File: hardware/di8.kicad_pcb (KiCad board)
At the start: 4 copper layers, 100 x 85 mm, 128 parts, among them J101 TNG-Power-TOP, J102 TNG-Power-BTM, J103 TNG-Data-TOP, J104 TNG-Data-BTM, P101 BOOT, P102 Debug, P103 PE, P201 INPUT0, P202 INPUT1, P203 INPUT2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

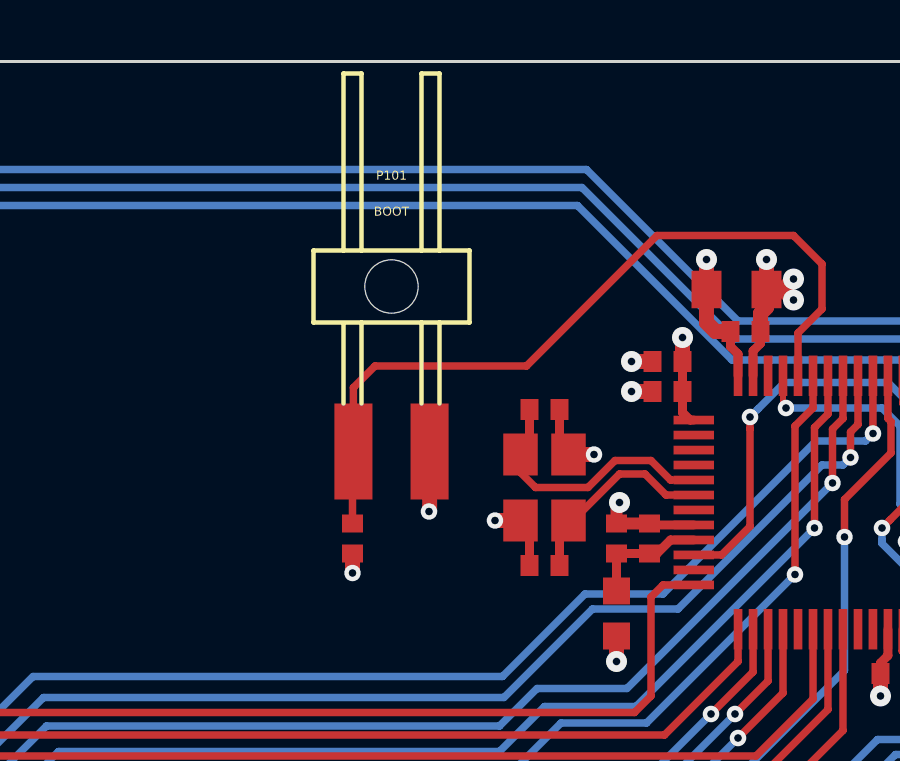
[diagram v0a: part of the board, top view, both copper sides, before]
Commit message: add boot switch
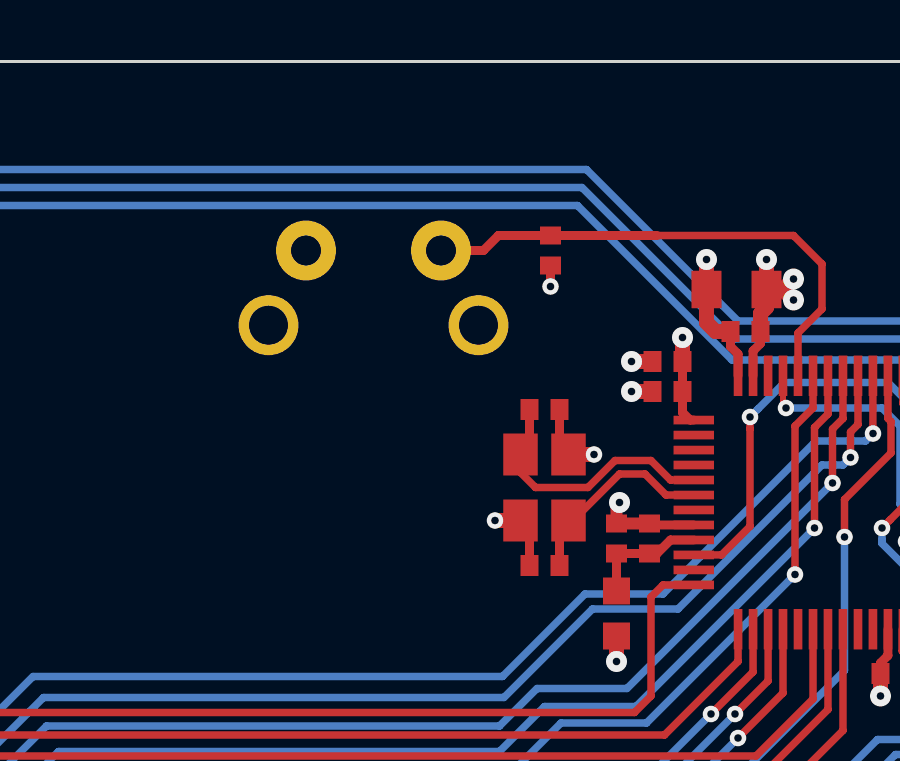
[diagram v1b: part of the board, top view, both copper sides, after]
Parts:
- removed P101: BOOT, pin_array_2x1_smd
- added SW101: BOOT, kicad-libraries:TACT-6MM-HOR, F.Cu at (143.8, 68.8)
- moved R101 11.6 mm to (149.7, 68.8)
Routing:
- net Net-(R101-Pad2): track 26.7 -> 17.4 mm
- net 3V3: track 56.9 -> 54.9 mm, vias 22 -> 21
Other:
- board text removed: "Was machen wir mit dem Jumper? Taster? -> Brick Taster Testpunkte?"

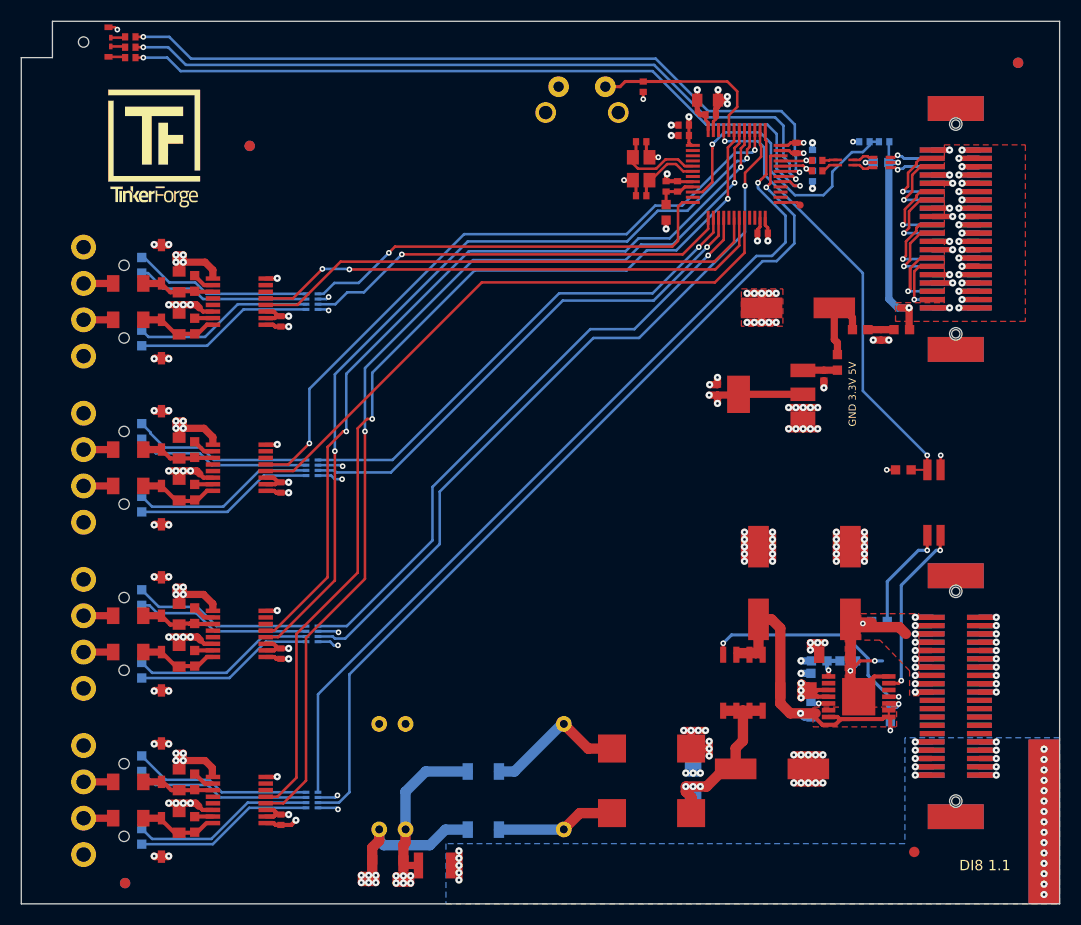
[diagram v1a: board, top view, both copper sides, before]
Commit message: improve lightpipes
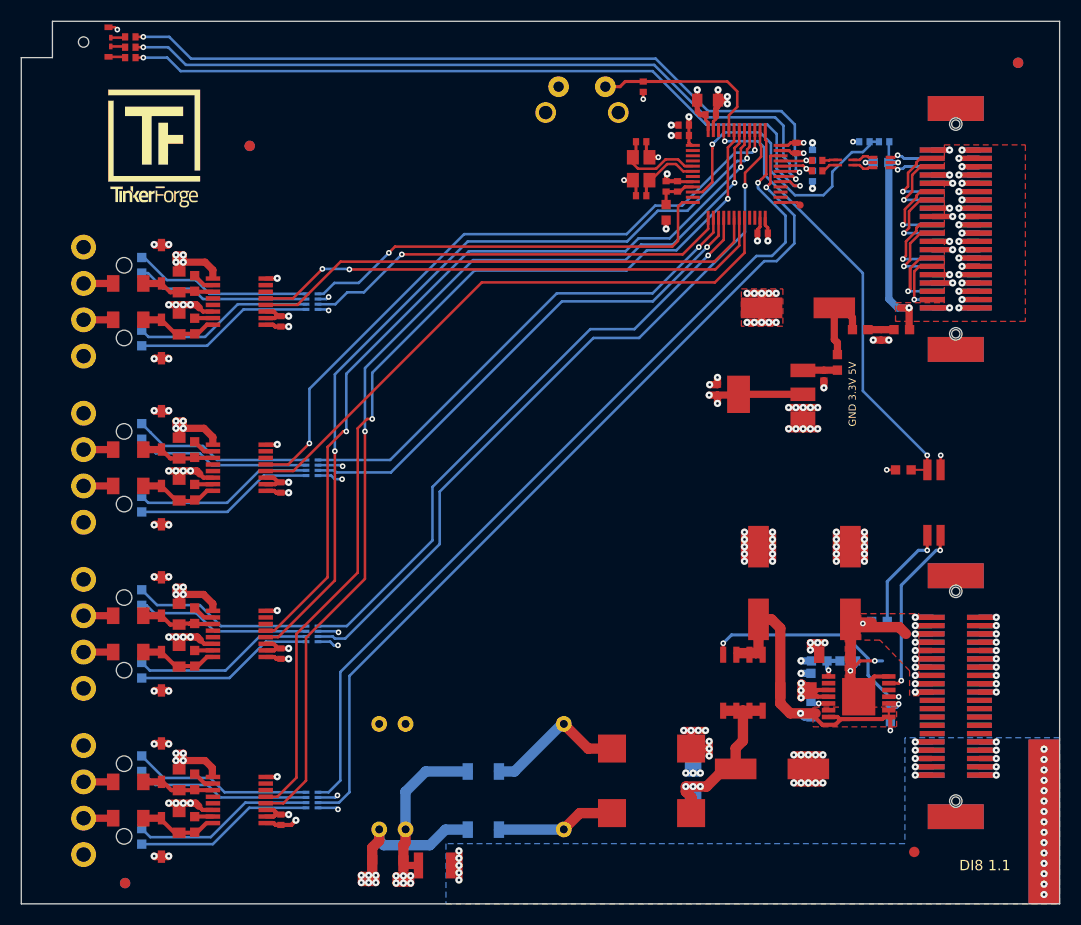
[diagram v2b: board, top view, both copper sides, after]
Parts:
- D203, D204, D205, D206, D207, D208, D209, D210: footprint LED-LP -> kicad-libraries:LED-LP
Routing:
- net LED6: track 84.8 -> 85.4 mm

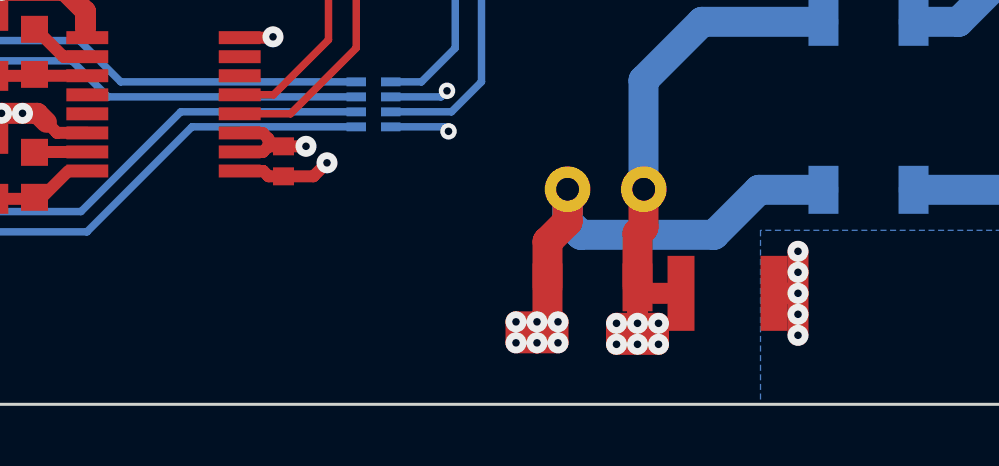
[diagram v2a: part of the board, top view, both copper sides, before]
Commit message: add vcc input protection
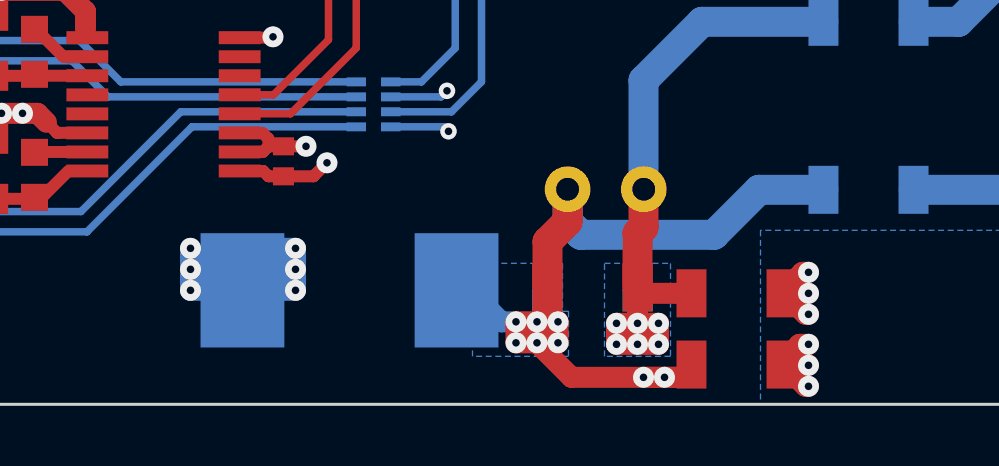
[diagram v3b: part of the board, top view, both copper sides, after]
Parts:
- removed C201: 500pF/2kV, C1210
- added C127: 4.7nF/2kV, C1206, F.Cu at (129.9, 146.2)
- added C128: 4.7nF/2kV, C1206, F.Cu at (129.9, 143.8)
- added D101: 3.0SMI30CATR, kicad-libraries:SMC, B.Cu at (117.0, 143.7)
- added R116: VC1206K201R030, kicad-libraries:R1206, B.Cu at (125.1, 143.6)
- C118: value 10µF/35V -> 10µF/50V
- D203, D204, D205, D206, D207, D208, D209, D210: footprint kicad-libraries:LED-LP -> LED-LP
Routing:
- net VCC: track 20.7 -> 31.1 mm, vias 6 -> 8
- net AGND: track 115.7 -> 123.3 mm, vias 54 -> 60
- net Earth: track 51.1 -> 54.1 mm, vias 30 -> 31
- added copper zone on B.Cu, net AGND
- added copper zone on B.Cu, net VCC

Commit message: outline update
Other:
- outline, holes or cut-outs redrawn
- board text added: "DI0"
- board text added: "DI1"
- board text added: "DI2"
- board text added: "DI3"
- board text added: "DI4"
- board text added: "DI5"
- board text added: "DI6"
- board text added: "DI7"
- board text added: "tinkerforge.com"
- board text removed: "DI 0"
- board text removed: "DI 1"
- board text removed: "DI 2"
- board text removed: "DI 3"
- board text removed: "DI 4"
- board text removed: "DI 5"
- board text removed: "DI 6"
- board text removed: "DI 7"
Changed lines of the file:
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@@
-(kicad_pcb (version 20171130) (host pcbnew 5.1.4-e60b266~84~ubuntu18.04.1)
+(kicad_pcb (version 20171130) (host pcbnew 5.1.5-52549c5~84~ubuntu18.04.1)
   (general
     (thickness 1.6)
-    (drawings 24)
+    (drawings 29)
     (tracks 1555)
     (zones 0)
@@
     )
   )
-  (gr_line (start 89.8 66) (end 89.8 147.5) (layer Edge.Cuts) (width 0.1))
+  (gr_text tinkerforge.com (at 180.8 144.5) (layer B.SilkS)
+    (effects (font (size 1 1) (thickness 0.2)) (justify mirror))
+  )
+  (gr_line (start 89.8 145.5) (end 89.8 147.5) (layer Edge.Cuts) (width 0.1))
+  (gr_line (start 89.8 81.5) (end 89.8 66) (layer Edge.Cuts) (width 0.1))
+  (gr_line (start 92.8 81.5) (end 89.8 81.5) (layer Edge.Cuts) (width 0.1))
+  (gr_line (start 92.8 145.5) (end 92.8 81.5) (layer Edge.Cuts) (width 0.1))
+  (gr_line (start 89.8 145.5) (end 92.8 145.5) (layer Edge.Cuts) (width 0.1))
   (gr_line (start 92.8 62.5) (end 189.8 62.5) (layer Edge.Cuts) (width 0.1))
   (gr_line (start 92.8 66) (end 89.8 66) (layer Edge.Cuts) (width 0.1))
@@
     (effects (font (size 0.7 0.7) (thickness 0.15)))
   )
-  (gr_text GND (at 93.9 142.8) (layer B.SilkS)
-    (effects (font (size 1 1) (thickness 0.15)) (justify left mirror))
+  (gr_text GND (at 93.9 142.8 90) (layer B.SilkS)
+    (effects (font (size 1 1) (thickness 0.15)) (justify mirror))
   )
-  (gr_text "DI 7" (at 93.8 139.4) (layer B.SilkS)
-    (effects (font (size 1 1) (thickness 0.15)) (justify left mirror))
+  (gr_text DI7 (at 93.8 139.2 90) (layer B.SilkS)
+    (effects (font (size 1 1) (thickness 0.15)) (justify mirror))
   )
-  (gr_text "DI 6" (at 93.8 135.9) (layer B.SilkS)
-    (effects (font (size 1 1) (thickness 0.15)) (justify left mirror))
+  (gr_text DI6 (at 93.8 135.8 90) (layer B.SilkS)
+    (effects (font (size 1 1) (thickness 0.15)) (justify mirror))
   )
-  (gr_text VCC (at 93.8 132.3) (layer B.SilkS)
-    (effects (font (size 1 1) (thickness 0.15)) (justify left mirror))
+  (gr_text VCC (at 93.8 132.3 90) (layer B.SilkS)
+    (effects (font (size 1 1) (thickness 0.15)) (justify mirror))
   )
-  (gr_text GND (at 93.8 126.8) (layer B.SilkS)
-    (effects (font (size 1 1) (thickness 0.15)) (justify left mirror))
+  (gr_text GND (at 93.8 126.8 90) (layer B.SilkS)
+    (effects (font (size 1 1) (thickness 0.15)) (justify mirror))
   )
-  (gr_text "DI 5" (at 93.8 123.3) (layer B.SilkS)
-    (effects (font (size 1 1) (thickness 0.15)) (justify left mirror))
+  (gr_text DI5 (at 93.8 123.3 90) (layer B.SilkS)
+    (effects (font (size 1 1) (thickness 0.15)) (justify mirror))
   )
-  (gr_text "DI 4" (at 93.8 119.8) (layer B.SilkS)
-    (effects (font (size 1 1) (thickness 0.15)) (justify left mirror))
+  (gr_text DI4 (at 93.8 119.8 90) (layer B.SilkS)
+    (effects (font (size 1 1) (thickness 0.15)) (justify mirror))
   )
-  (gr_text VCC (at 93.8 116.2) (layer B.SilkS)
-    (effects (font (size 1 1) (thickness 0.15)) (justify left mirror))
+  (gr_text VCC (at 93.8 116.2 90) (layer B.SilkS)
+    (effects (font (size 1 1) (thickness 0.15)) (justify mirror))
   )
-  (gr_text GND (at 93.8 110.8) (layer B.SilkS)
-    (effects (font (size 1 1) (thickness 0.15)) (justify left mirror))
+  (gr_text GND (at 93.8 110.8 90) (layer B.SilkS)
+    (effects (font (size 1 1) (thickness 0.15)) (justify mirror))
   )
-  (gr_text "DI 3" (at 93.8 107.3) (layer B.SilkS)
-    (effects (font (size 1 1) (thickness 0.15)) (justify left mirror))
+  (gr_text DI3 (at 93.8 107.3 90) (layer B.SilkS)
+    (effects (font (size 1 1) (thickness 0.15)) (justify mirror))
   )
-  (gr_text "DI 2" (at 93.8 103.8) (layer B.SilkS)
-    (effects (font (size 1 1) (thickness 0.15)) (justify left mirror))
+  (gr_text DI2 (at 93.8 103.8 90) (layer B.SilkS)
+    (effects (font (size 1 1) (thickness 0.15)) (justify mirror))
   )
-  (gr_text VCC (at 93.8 100.3) (layer B.SilkS)
-    (effects (font (size 1 1) (thickness 0.15)) (justify left mirror))
+  (gr_text VCC (at 93.8 100.3 90) (layer B.SilkS)
+    (effects (font (size 1 1) (thickness 0.15)) (justify mirror))
   )
-  (gr_text GND (at 93.8 94.8) (layer B.SilkS)
-    (effects (font (size 1 1) (thickness 0.15)) (justify left mirror))
+  (gr_text GND (at 93.8 94.8 90) (layer B.SilkS)
+    (effects (font (size 1 1) (thickness 0.15)) (justify mirror))
   )
-  (gr_text "DI 1" (at 93.8 91.3) (layer B.SilkS)
-    (effects (font (size 1 1) (thickness 0.15)) (justify left mirror))
+  (gr_text DI1 (at 93.8 91.3 90) (layer B.SilkS)
+    (effects (font (size 1 1) (thickness 0.15)) (justify mirror))
   )
-  (gr_text VCC (at 93.8 84.2) (layer B.SilkS)
-    (effects (font (size 1 1) (thickness 0.15)) (justify left mirror))
+  (gr_text VCC (at 93.8 84.2 90) (layer B.SilkS)
+    (effects (font (size 1 1) (thickness 0.15)) (justify mirror))
   )
-  (gr_text "DI 0" (at 93.8 87.9) (layer B.SilkS)
-    (effects (font (size 1 1) (thickness 0.15)) (justify left mirror))
+  (gr_text DI0 (at 93.8 87.8 90) (layer B.SilkS)
+    (effects (font (size 1 1) (thickness 0.15)) (justify mirror))
   )
-  (gr_text "DI8 1.1" (at 182.6 143.8) (layer F.SilkS)
+  (gr_text "DI8 1.1" (at 180.8 144.5) (layer F.SilkS)
     (effects (font (size 1 1) (thickness 0.15)))
   )

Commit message: fix name
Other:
- board text added: "DI 8P REV 1.1"
- board text removed: "DI8 1.1"
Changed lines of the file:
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@@
     (effects (font (size 1 1) (thickness 0.15)) (justify mirror))
   )
-  (gr_text "DI8 1.1" (at 180.8 144.5) (layer F.SilkS)
+  (gr_text "DI 8P\nREV 1.1" (at 180.8 144.5) (layer F.SilkS)
     (effects (font (size 1 1) (thickness 0.15)))
   )

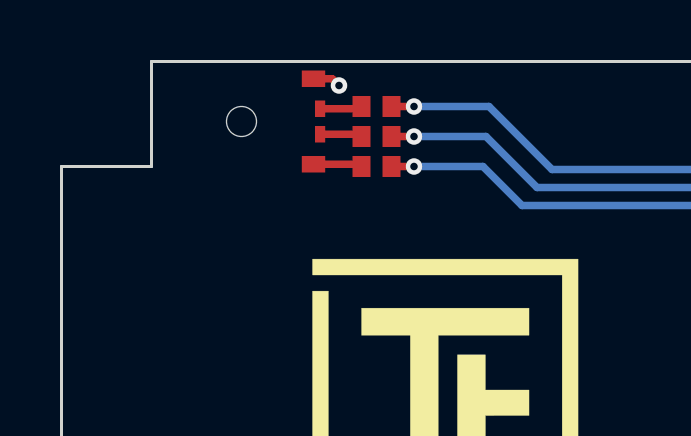
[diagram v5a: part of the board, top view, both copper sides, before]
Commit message: update rgb led drill diameter
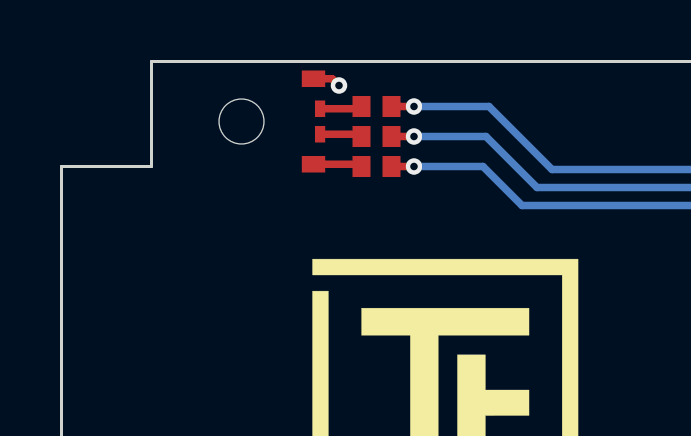
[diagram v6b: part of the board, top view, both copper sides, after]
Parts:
- LED101: footprint LED-RGB-LP -> kicad-libraries:LED-RGB-LP
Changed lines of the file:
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@@
     (add_net USB-DPC)
   )
+  (module kicad-libraries:LED-RGB-LP (layer F.Cu)
+    (at 98.2 64.5 90)
+    (fp_text reference LED101 (at 0 0 90) (layer F.Fab)
+      (effects (font (size 0.15 0.15) (thickness 0.0375)))
+    )
+    (fp_text value EASV3015RGBA0 (at 0 -0.3 90) (layer F.Fab)
+      (effects (font (size 0.15 0.15) (thickness 0.0375)))
+    )
+    (fp_line (start -1 -1.4) (end 1 -1.4) (layer F.Fab) (width 0.1))
+    (fp_line (start 1 -1.4) (end 1 -8.4) (layer F.Fab) (width 0.1))
+    (fp_line (start 1 -8.4) (end -1 -8.4) (layer F.Fab) (width 0.1))
+    (fp_line (start -1 -8.4) (end -1 -1.4) (layer F.Fab) (width 0.1))
+    (fp_line (start -1.5 -0.5) (end -1.5 0.2) (layer F.Fab) (width 0.025))
+    (fp_line (start 1.5 -0.5) (end -1.5 -0.5) (layer F.Fab) (width 0.025))
+    (fp_line (start 1.5 0.2) (end 1.5 -0.5) (layer F.Fab) (width 0.025))
+    (fp_line (start -1.5 0.2) (end 1.5 0.2) (layer F.Fab) (width 0.025))
+    (fp_arc (start 0 -0.5) (end -0.8 -0.5) (angle 90) (layer F.Fab) (width 0.025))
+    (fp_arc (start 0 -0.5) (end 0 -1.3) (angle 90) (layer F.Fab) (width 0.025))
+    (pad 3 smd rect (at -0.425 0.22 90) (size 0.55 0.34) (layers F.Cu F.Paste F.Mask)
+      (net 49 "Net-(LED101-Pad3)"))
+    (pad 2 smd rect (at 0.425 0.22 90) (size 0.55 0.34) (layers F.Cu F.Paste F.Mask)
+      (net 48 "Net-(LED101-Pad2)"))
+    (pad 4 smd rect (at -1.425 0 90) (size 0.55 0.78) (layers F.Cu F.Paste F.Mask)
+      (net 47 "Net-(LED101-Pad4)"))
+    (pad 1 smd rect (at 1.425 0 90) (size 0.55 0.78) (layers F.Cu F.Paste F.Mask)
+      (net 2 3V3))
+    (pad "" np_thru_hole circle (at 0 -2.4 90) (size 1.5 1.5) (drill 1.5) (layers *.Cu *.Mask))
+  )
   (module kicad-libraries:Fiducial_Mark (layer B.Cu)
     (at 99.8 145.5)
@@
     )
   )
-  (module LED-RGB-LP (layer F.Cu)
-    (at 98.2 64.5 90)
-    (fp_text reference LED101 (at 0 0 90) (layer F.Fab)
-      (effects (font (size 0.15 0.15) (thickness 0.0375)))
-    )
-    (fp_text value EASV3015RGBA0 (at 0 -0.3 90) (layer F.Fab)
-      (effects (font (size 0.15 0.15) (thickness 0.0375)))
-    )
-    (fp_arc (start 0 -0.5) (end 0 -1.3) (angle 90) (layer F.Fab) (width 0.025))
-    (fp_arc (start 0 -0.5) (end -0.8 -0.5) (angle 90) (layer F.Fab) (width 0.025))
-    (fp_line (start -1.5 0.2) (end 1.5 0.2) (layer F.Fab) (width 0.025))
-    (fp_line (start 1.5 0.2) (end 1.5 -0.5) (layer F.Fab) (width 0.025))
-    (fp_line (start 1.5 -0.5) (end -1.5 -0.5) (layer F.Fab) (width 0.025))
-    (fp_line (start -1.5 -0.5) (end -1.5 0.2) (layer F.Fab) (width 0.025))
-    (fp_line (start -1 -8.4) (end -1 -1.4) (layer F.Fab) (width 0.1))
-    (fp_line (start 1 -8.4) (end -1 -8.4) (layer F.Fab) (width 0.1))
-    (fp_line (start 1 -1.4) (end 1 -8.4) (layer F.Fab) (width 0.1))
-    (fp_line (start -1 -1.4) (end 1 -1.4) (layer F.Fab) (width 0.1))
-    (pad "" np_thru_hole circle (at 0 -2.4 90) (size 1 1) (drill 1) (layers *.Cu *.Mask))
-    (pad 1 smd rect (at 1.425 0 90) (size 0.55 0.78) (layers F.Cu F.Paste F.Mask)
-      (net 2 3V3))
-    (pad 4 smd rect (at -1.425 0 90) (size 0.55 0.78) (layers F.Cu F.Paste F.Mask)
-      (net 47 "Net-(LED101-Pad4)"))
-    (pad 2 smd rect (at 0.425 0.22 90) (size 0.55 0.34) (layers F.Cu F.Paste F.Mask)
-      (net 48 "Net-(LED101-Pad2)"))
-    (pad 3 smd rect (at -0.425 0.22 90) (size 0.55 0.34) (layers F.Cu F.Paste F.Mask)
-      (net 49 "Net-(LED101-Pad3)"))
-  )
   (module kicad-libraries:Logo_TF_10x12 (layer F.Cu)
